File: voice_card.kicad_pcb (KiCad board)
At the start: 2 copper layers, 133.3 x 30 mm, 207 parts, among them J1 DDR3-DIMM, Q1 MMBF4391LT1G, Q10 DMMT3906, Q11 BC857BS, Q2 2N3904, Q3 BCM847, Q4 DMMT3904, Q5 DMMT3906, Q6 MMBF4391LT1G, Q7 BCM847, Q8 2N3904, Q9 DMMT3904, U1 TL074-, U10 TL072-, U11 TL074-, U12 NE555, U13 LM311M, U14 CD4052, U15 TL072-, U16 TL072-, U17 LM13700, U18 LM13700, U19 LM13700, U2 TL074-, U20 TL072-, U3 NE555, U4 LF351, U5 TL072-, U6 LM311M, U7 CD4052, U8 TL074-, U9 LF351

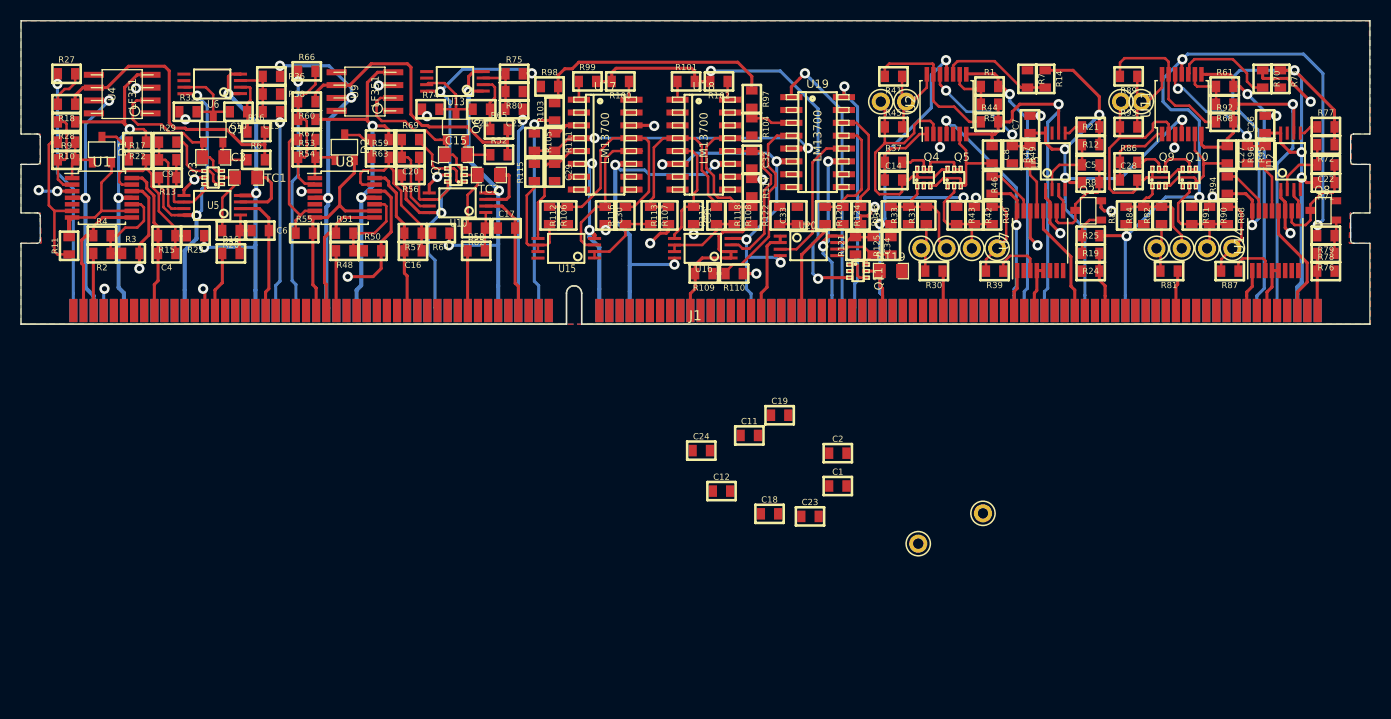
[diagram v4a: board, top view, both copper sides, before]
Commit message: decoupling caps placed and routed. Still stitching ground plane
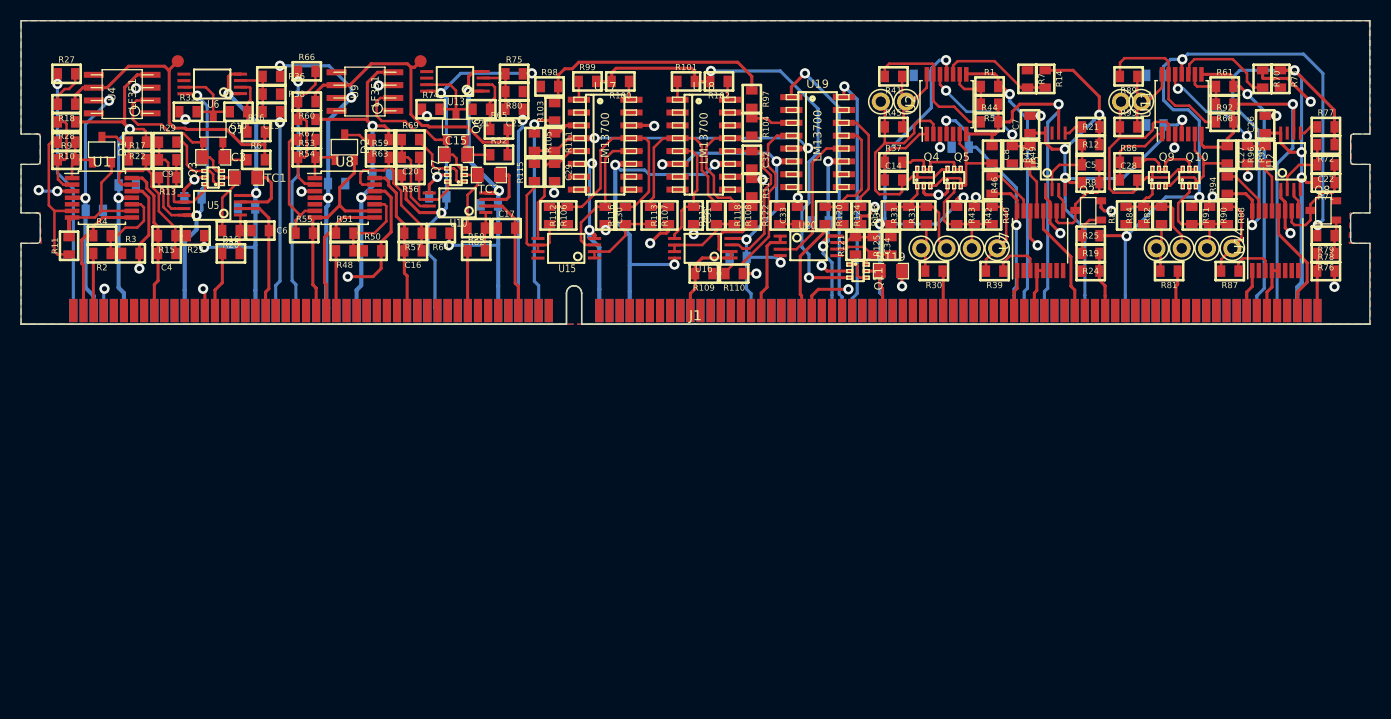
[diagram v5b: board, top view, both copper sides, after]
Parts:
- added C35: 100n, MyModules:SM0603-C-JRL, B.Cu at (80.8, 79.2)
- added C36: 100n, MyModules:SM0603-C-JRL, B.Cu at (84.0, 76.8)
- added C37: 100n, MyModules:SM0603-C-JRL, B.Cu at (104.7, 76.6)
- added C38: 100n, MyModules:SM0603-C-JRL, B.Cu at (109.1, 75.7)
- added C39: 100n, MyModules:SM0603-C-JRL, B.Cu at (152.5, 80.4)
- added C40: 100n, MyModules:SM0603-C-JRL, B.Cu at (144.4, 83.9)
- C1, C11, C12, C18, C19, C2, C23, C24: moved to B.Cu
- TP1, TP8: footprint MyModules:TEST_POINT_5000_SERIES -> MyModules:TEST_PAD
- moved TP1 87.4 mm to (89.0, 64.5)
- moved TP8 71.3 mm to (113.0, 64.5)
- moved C1 69.8 mm to (90.5, 78.0), turned to 180 degrees
- moved C2 63.3 mm to (95.8, 79.0)
- moved C24 58.2 mm to (185.6, 65.9)
- moved C23 51.6 mm to (185.6, 70.8), turned to 180 degrees
- moved C18 40.9 mm to (166.4, 73.0), turned to 180 degrees
- moved C11 38.8 mm to (114.7, 77.9), turned to 180 degrees
- moved C19 36.4 mm to (162.6, 65.9)
- moved C12 36.4 mm to (119.8, 78.7)
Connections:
- J1 pad 164: Net-(J1-Pad164) -> GND
- J1 pad 78: Net-(J1-Pad78) -> GND
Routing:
- net GND: track 99.0 -> 117.8 mm, vias 31 -> 39
- net +12V: track 340.4 -> 354.0 mm
- net -12V: track 308.0 -> 315.0 mm
- net Net-(R18-Pad1): track 29.8 -> 31.1 mm
- net Iabc: track 47.1 -> 48.4 mm
- net Net-(R52-Pad2): track 30.2 -> 31.4 mm

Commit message: placed silkscreen component references. still need to finish up ground stitching
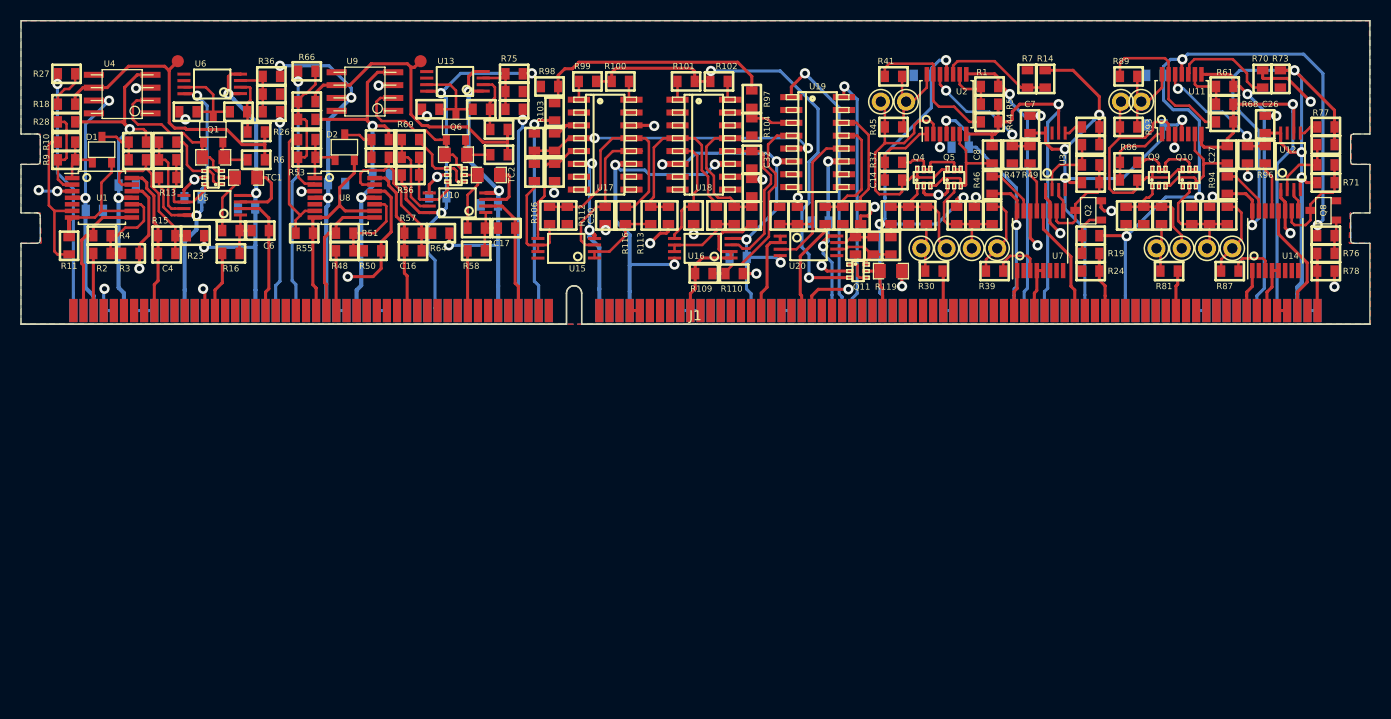
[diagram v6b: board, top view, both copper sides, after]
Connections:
- J1 pad 108: Net-(J1-Pad108) -> GND
- J1 pad 109: Net-(J1-Pad109) -> GND
- J1 pad 134: Net-(J1-Pad134) -> GND
- J1 pad 173: Net-(J1-Pad173) -> GND
- J1 pad 190: Net-(J1-Pad190) -> GND
- J1 pad 198: Net-(J1-Pad198) -> GND
- J1 pad 220: Net-(J1-Pad220) -> GND
- J1 pad 222: Net-(J1-Pad222) -> GND
- J1 pad 223: Net-(J1-Pad223) -> GND
- J1 pad 237: Net-(J1-Pad237) -> GND
- J1 pad 28: Net-(J1-Pad28) -> GND
- J1 pad 48: Net-(J1-Pad48) -> GND
- J1 pad 57: Net-(J1-Pad57) -> GND
- J1 pad 7: Net-(J1-Pad7) -> GND
- J1 pad 75: Net-(J1-Pad75) -> GND
- J1 pad 8: Net-(J1-Pad8) -> GND
- J1 pad 84: Net-(J1-Pad84) -> GND
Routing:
- net GND: track 117.8 -> 130.8 mm

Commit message: stitching done. 21 unconnected, all of which should be resolved by connecting pins on J1
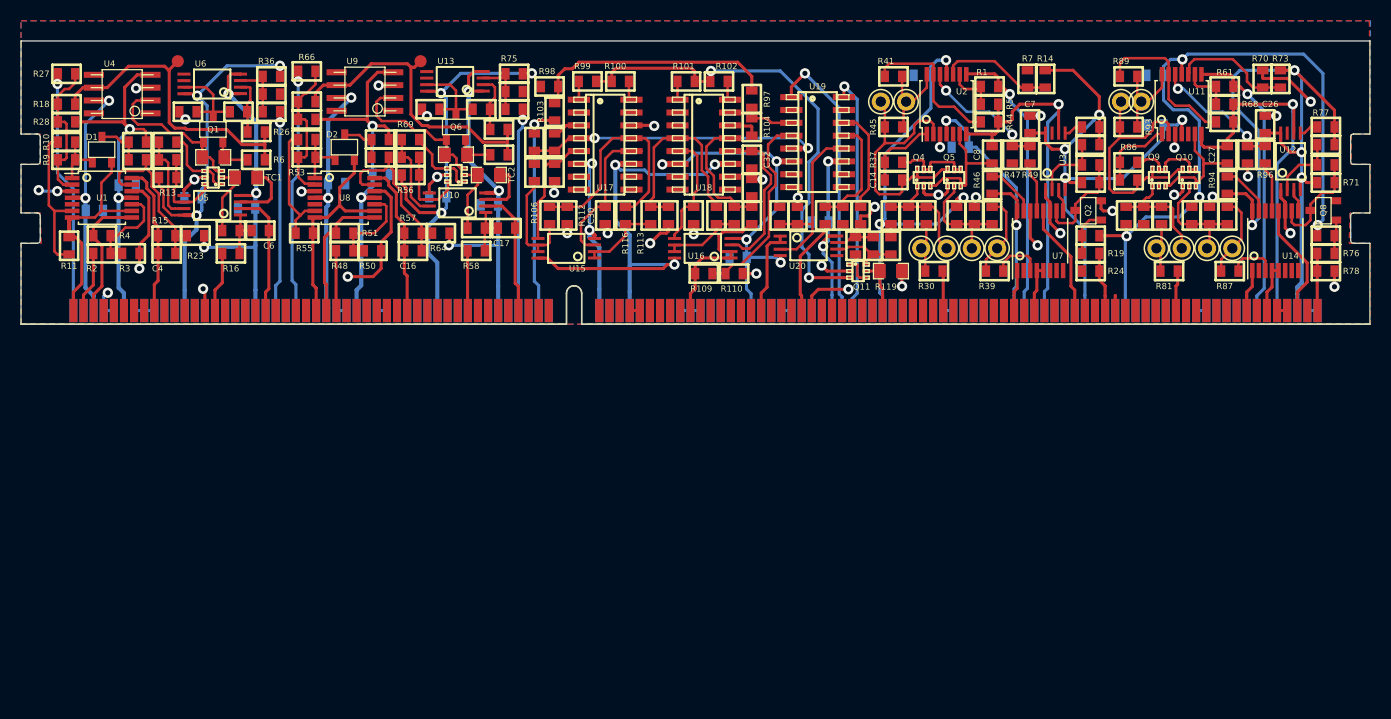
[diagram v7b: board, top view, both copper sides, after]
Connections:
- J1 pad 2: VCO1_PULSE -> VCO1_PWM_CV
- J1 pad 214: Net-(J1-Pad214) -> GND
- J1 pad 3: VCO1_PWM_CV -> VCO1_PULSE
- J1 pad 91: Net-(J1-Pad91) -> GND
- J1 pad 94: Net-(J1-Pad94) -> GND
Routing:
- net +12V: track 354.0 -> 368.6 mm
- net VCO1_SAW: track 13.4 -> 21.9 mm
- net GND: track 130.8 -> 138.3 mm, vias 39 -> 41
- net Net-(R70-Pad2): track 10.1 -> 11.9 mm
- net Net-(R18-Pad2): track 13.0 -> 14.7 mm
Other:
- board size 133.3 x 30 mm -> 133.3 x 28 mm

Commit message: made connections on DIMM socket bilaterally symmetrical and started to route accordingly
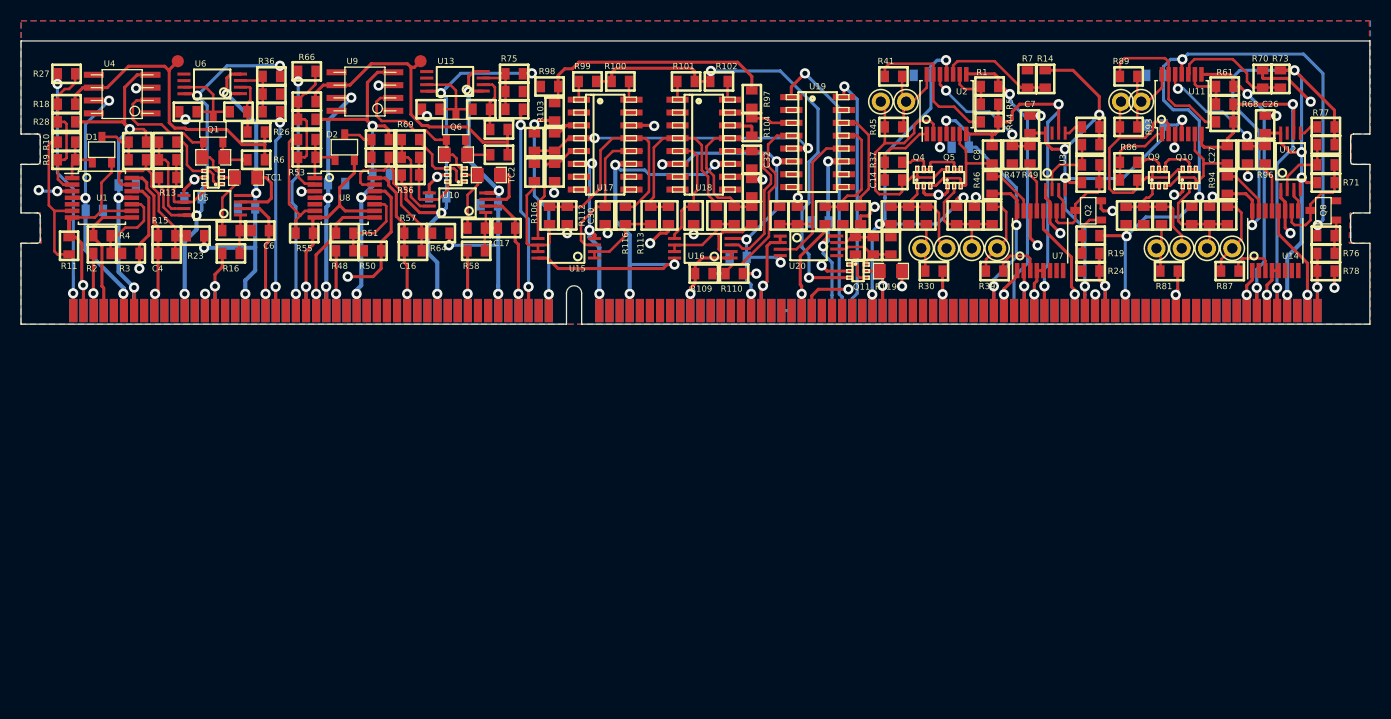
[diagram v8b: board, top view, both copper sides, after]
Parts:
- J1: moved to B.Cu
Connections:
- J1 pad 1: VCO1_SAW -> VCO1_TRI_SHAPE
- J1 pad 10: Net-(J1-Pad10) -> GND
- J1 pad 101: Net-(J1-Pad101) -> -12V
- J1 pad 11: Net-(J1-Pad11) -> GND
- J1 pad 110: Net-(J1-Pad110) -> GND
- J1 pad 111: Net-(J1-Pad111) -> GND
- J1 pad 112: Net-(J1-Pad112) -> GND
- J1 pad 114: GND -> EG2_INV_OUT
- J1 pad 116: GND -> EG2_ENV_OUT
- J1 pad 117: GND -> +12V
- J1 pad 118: EG2_SUSTAIN_CV -> GND
- J1 pad 119: GND -> EG2_SUSTAIN_CV
- J1 pad 12: GND -> +12V
- J1 pad 122: Net-(J1-Pad122) -> VCO1_SAW
- J1 pad 123: +12V -> VCO1_PWM_CV
- J1 pad 124: GND -> VCO1_PULSE
- J1 pad 126: -12V -> +12V
- J1 pad 127: GND -> -12V
- J1 pad 129: GND -> VCO1_TRI
- J1 pad 13: Net-(J1-Pad13) -> GND
- J1 pad 130: Net-(J1-Pad130) -> GND
- J1 pad 131: Net-(J1-Pad131) -> GND
- J1 pad 133: Net-(J1-Pad133) -> GND
- J1 pad 135: GND -> VCO1_SCALE
- J1 pad 138: Net-(J1-Pad138) -> -12V
- J1 pad 139: -12V -> GND
- J1 pad 140: GND -> VCO1_PITCH_CV
- J1 pad 144: Net-(J1-Pad144) -> VCO2_SAW
- J1 pad 145: Net-(J1-Pad145) -> VCO2_PULSE
- J1 pad 147: GND -> VCO2_PWM_CV
- J1 pad 150: Net-(J1-Pad150) -> GND
- J1 pad 153: Net-(J1-Pad153) -> GND
- J1 pad 154: Net-(J1-Pad154) -> VCO2_TRI
- J1 pad 160: GND -> VCO2_SCALE
- J1 pad 165: VCO2_SYNC_IN -> VCO2_PITCH_CV
- J1 pad 166: GND -> VCO2_SYNC_IN
- J1 pad 167: VCF_IN -> GND
- J1 pad 168: GND -> VCF_IN
- J1 pad 178: GND -> VCF_OUT
- J1 pad 18: Net-(J1-Pad18) -> -12V
- J1 pad 185: Net-(J1-Pad185) -> VCA_OUT
- J1 pad 186: Net-(J1-Pad186) -> GND
- J1 pad 189: Net-(J1-Pad189) -> VCA_IN
- J1 pad 19: Net-(J1-Pad19) -> GND
- J1 pad 196: Net-(J1-Pad196) -> -12V
- J1 pad 197: -12V -> VCF_CTRL
- J1 pad 2: VCO1_PWM_CV -> VCO1_SAW
- J1 pad 203: GND -> EG1_ATTACK_CV
- J1 pad 208: Net-(J1-Pad208) -> +12V
- J1 pad 209: Net-(J1-Pad209) -> EG1_DECAY_CV
- J1 pad 21: GND -> VCO1_SYNC_IN
- J1 pad 210: +12V -> EG1_INV_OUT
- J1 pad 211: EG1_INV_OUT -> GND
- J1 pad 212: GND -> EG1_RELEASE_CV
- J1 pad 215: Net-(J1-Pad215) -> GND
- J1 pad 216: Net-(J1-Pad216) -> EG1_SUSTAIN_CV
- J1 pad 218: Net-(J1-Pad218) -> GND
- J1 pad 219: GND -> EG1_GATE
- J1 pad 22: Net-(J1-Pad22) -> GND
- J1 pad 226: Net-(J1-Pad226) -> EG2_ATTACK_CV
- J1 pad 23: Net-(J1-Pad23) -> VCO2_TRI_SHAPE
- J1 pad 230: Net-(J1-Pad230) -> GND
- J1 pad 231: Net-(J1-Pad231) -> GND
- J1 pad 232: Net-(J1-Pad232) -> GND
- J1 pad 233: Net-(J1-Pad233) -> EG2_DECAY_CV
- J1 pad 235: GND -> EG2_RELEASE_CV
- J1 pad 237: GND -> +12V
- J1 pad 238: +12V -> GND
- J1 pad 239: GND -> EG2_SUSTAIN_CV
- J1 pad 24: Net-(J1-Pad24) -> VCO2_SAW
- J1 pad 240: GND -> EG2_GATE
- J1 pad 25: VCO2_SAW -> VCO2_PULSE
- J1 pad 26: VCO2_PULSE -> +12V
- J1 pad 29: Net-(J1-Pad29) -> -12V
- J1 pad 3: VCO1_PULSE -> VCO1_PWM_CV
- J1 pad 30: Net-(J1-Pad30) -> GND
- J1 pad 31: Net-(J1-Pad31) -> GND
- J1 pad 32: Net-(J1-Pad32) -> GND
- J1 pad 33: Net-(J1-Pad33) -> GND
- J1 pad 37: Net-(J1-Pad37) -> +12V
- J1 pad 4: GND -> VCO1_PULSE
- J1 pad 43: Net-(J1-Pad43) -> -12V
- J1 pad 46: GND -> VCO2_SYNC_IN
- J1 pad 47: Net-(J1-Pad47) -> GND
- J1 pad 48: GND -> VCF_IN
- J1 pad 49: Net-(J1-Pad49) -> -12V
- J1 pad 52: GND -> +12V
- J1 pad 6: Net-(J1-Pad6) -> +12V
- J1 pad 64: Net-(J1-Pad64) -> -12V
- J1 pad 67: Net-(J1-Pad67) -> GND
- J1 pad 68: Net-(J1-Pad68) -> GND
- J1 pad 7: GND -> -12V
- J1 pad 72: Net-(J1-Pad72) -> +12V
- J1 pad 73: Net-(J1-Pad73) -> RES_CTRL
- J1 pad 74: Net-(J1-Pad74) -> VCA_CTRL
- J1 pad 76: Net-(J1-Pad76) -> -12V
- J1 pad 88: Net-(J1-Pad88) -> +12V
- J1 pad 89: Net-(J1-Pad89) -> EG1_DECAY_CV
- J1 pad 90: EG1_DECAY_CV -> EG1_INV_OUT
- J1 pad 93: Net-(J1-Pad93) -> EG1_ENV_OUT
- J1 pad 95: Net-(J1-Pad95) -> GND
- J1 pad 97: GND -> +12V
- J1 pad 98: Net-(J1-Pad98) -> GND
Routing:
- net +12V: track 368.6 -> 386.1 mm, vias 25 -> 33
- net -12V: track 315.1 -> 328.6 mm, vias 23 -> 31
- net GND: track 138.3 -> 130.4 mm, vias 41 -> 42
- net VCF_CTRL: track 5.38 -> 8.06 mm, vias 0 -> 1
- net VCO2_SYNC_IN: track 20.1 -> 22.7 mm, vias 1 -> 2
- net VCA_OUT: track 8.69 -> 11.2 mm, vias 0 -> 1
- net VCO2_SAW: track 21.1 -> 23.6 mm, vias 0 -> 1
- net EG1_GATE: track 5.89 -> 8.34 mm, vias 0 -> 1
- net EG1_ENV_OUT: track 38.1 -> 40.5 mm, vias 1 -> 2
- net VCO1_SCALE: track 5.95 -> 8.35 mm, vias 0 -> 1
- net VCO1_SYNC_IN: track 19.8 -> 22.2 mm, vias 1 -> 2
- net EG2_GATE: track 5.66 -> 7.97 mm, vias 0 -> 1
- net VCO1_SAW: track 21.9 -> 24.2 mm, vias 0 -> 1
- net EG2_INV_OUT: track 28.3 -> 30.5 mm, vias 1 -> 2
- net EG2_ENV_OUT: track 38.0 -> 40.2 mm, vias 1 -> 2
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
